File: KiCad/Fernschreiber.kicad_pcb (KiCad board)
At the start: 2 copper layers, 100 x 100 mm, 40 parts, among them J1 Teleprinter, J10 Test_Conn_write, J11 Test_Conn_Lesen_b_opto, J12 Conn_01x05_Male, J2 Step-Up, J3 18,19,23,3V3,GND, J4 12,13,14,3V3,GND, J5 TX,RX,3V3,GND, J6 5V, J7 Test_Conn_3V3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

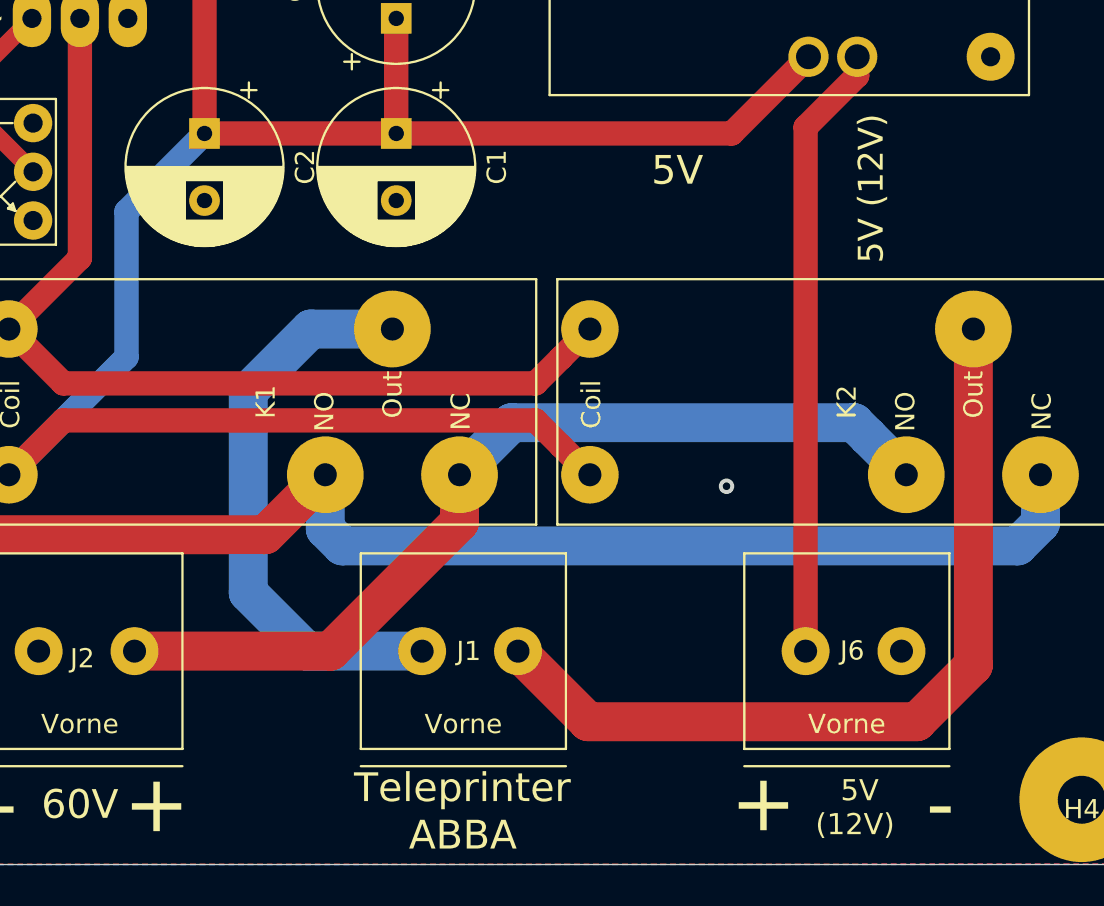
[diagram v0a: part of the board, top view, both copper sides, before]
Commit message: changed connector Position
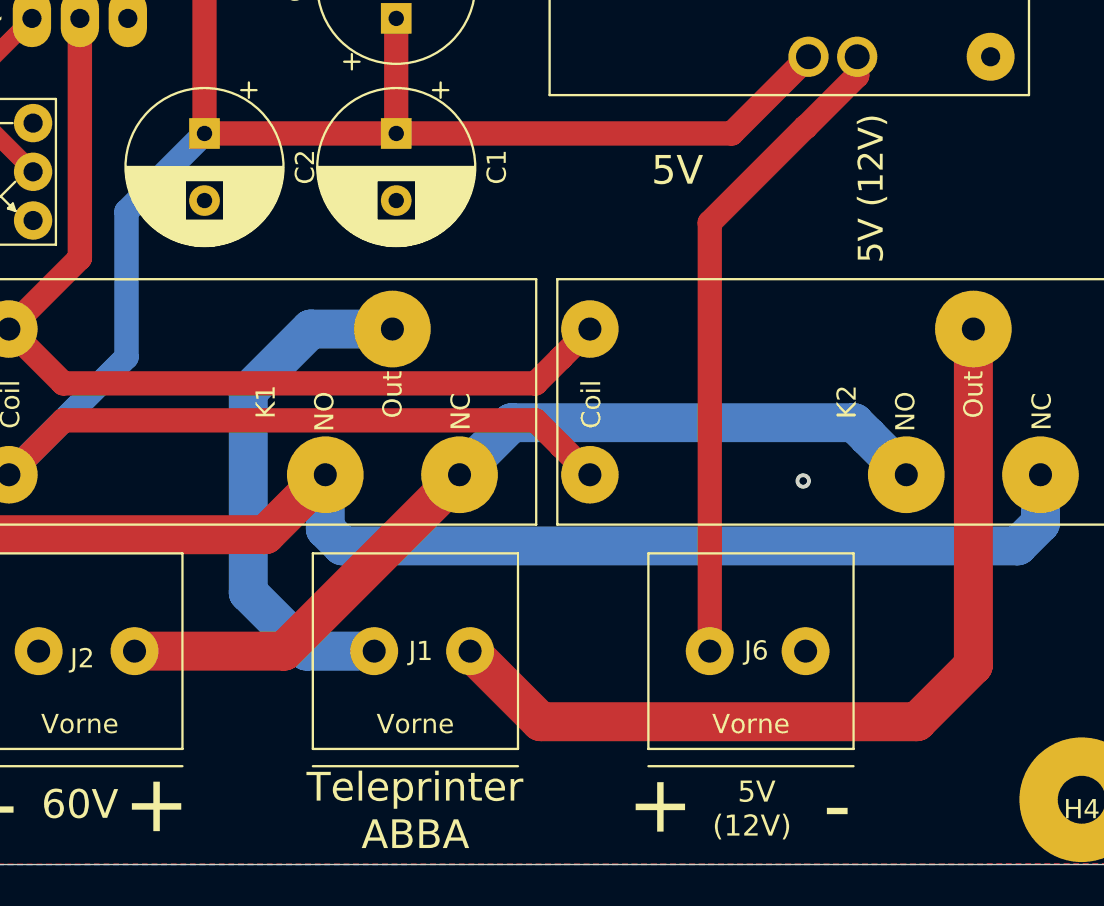
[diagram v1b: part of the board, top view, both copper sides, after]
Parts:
- moved J6 5.00 mm to (125.0, 130.0)
- moved J1 2.50 mm to (107.5, 130.0)
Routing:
- net Net-(J1-Pad1): track 29.7 -> 27.2 mm
- net Net-(J1-Pad2): track 44.0 -> 46.5 mm
- net /5V_12V: track 32.1 -> 34.2 mm
- net /Step-up_input: track 47.8 -> 46.3 mm
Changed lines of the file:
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@@
     (thickness 1.6)
     (drawings 37)
-    (tracks 158)
+    (tracks 159)
     (zones 0)
     (modules 40)
@@
   )
   (layers
-    (0 F.Cu signal hide)
-    (31 B.Cu signal hide)
-    (32 B.Adhes user hide)
-    (33 F.Adhes user hide)
+    (0 F.Cu signal)
+    (31 B.Cu signal)
+    (32 B.Adhes user)
+    (33 F.Adhes user)
     (34 B.Paste user)
-    (35 F.Paste user hide)
+    (35 F.Paste user)
     (36 B.SilkS user)
     (37 F.SilkS user)
@@
     (40 Dwgs.User user hide)
     (41 Cmts.User user hide)
-    (42 Eco1.User user hide)
-    (43 Eco2.User user hide)
+    (42 Eco1.User user)
+    (43 Eco2.User user)
     (44 Edge.Cuts user)
     (45 Margin user hide)
@@
   )
   (setup
-    (last_trace_width 0.25)
+    (last_trace_width 2.032)
     (user_trace_width 0.889)
     (user_trace_width 1.27)
@@
       (drillshape 0)
       (scaleselection 1)
-      (outputdirectory "Gerber/"))
+      (outputdirectory "Gerber_rev2/"))
   )
   (net 0 "")
@@
   (module Fernschreiber:HTR_Logo (layer F.Cu)
     (at 65.95 62.925)
-    (fp_text reference G*** (at -0.254 -14.097) (layer F.SilkS) hide
+    (fp_text reference G*** (at -0.254 -14.097) (layer Dwgs.User) hide
       (effects (font (size 1.524 1.524) (thickness 0.3)))
     )
-    (fp_text value LOGO (at -0.127 -12.065) (layer F.SilkS) hide
+    (fp_text value LOGO (at -0.127 -12.065) (layer Dwgs.User) hide
       (effects (font (size 1.524 1.524) (thickness 0.3)))
     )
@@
   (module Fernschreiber:Signatur (layer F.Cu)
     (at 128.225 46.675 90)
-    (fp_text reference G*** (at 0 0 90) (layer F.SilkS) hide
+    (fp_text reference G*** (at 0 0 90) (layer Dwgs.User) hide
       (effects (font (size 1.524 1.524) (thickness 0.3)))
     )
-    (fp_text value LOGO (at 0.75 0 90) (layer F.SilkS) hide
+    (fp_text value LOGO (at 0.75 0 90) (layer Dwgs.User) hide
       (effects (font (size 1.524 1.524) (thickness 0.3)))
     )
@@
   )
   (module "Fernschreiber:DECA MB310-500M02 Schraubklemmblock" (layer F.Cu)
-    (at 130 130)
+    (at 125 130)
     (fp_text reference J6 (at 0.2794 -0.0254) (layer F.SilkS)
       (effects (font (size 1 1) (thickness 0.15)))
@@
   )
   (module "Fernschreiber:DECA MB310-500M02 Schraubklemmblock" (layer F.Cu)
-    (at 110 130)
+    (at 107.5 130)
     (fp_text reference J1 (at 0.2794 0) (layer F.SilkS)
       (effects (font (size 1 1) (thickness 0.15)))
@@
     )
   )
-  (gr_text ABBA (at 109.975 139.6) (layer F.SilkS)
+  (gr_text ABBA (at 107.5 139.575) (layer F.SilkS)
     (effects (font (size 1.5 1.5) (thickness 0.3)))
   )
@@
     (effects (font (size 3 3) (thickness 0.5)))
   )
-  (gr_text - (at 134.875 138) (layer F.SilkS)
+  (gr_text - (at 129.5 138.075) (layer F.SilkS)
     (effects (font (size 3 3) (thickness 0.5)))
   )
-  (gr_text + (at 125.65 137.95) (layer F.SilkS)
+  (gr_text + (at 120.275 138.025) (layer F.SilkS)
     (effects (font (size 3 3) (thickness 0.5)))
   )
@@
     (effects (font (size 1.5 1.5) (thickness 0.3)))
   )
-  (gr_text Teleprinter (at 109.95 137.125) (layer F.SilkS)
+  (gr_text Teleprinter (at 107.475 137.1) (layer F.SilkS)
     (effects (font (size 1.5 1.5) (thickness 0.3)))
   )
@@
     (effects (font (size 1.5 1.5) (thickness 0.3)) (justify left mirror))
   )
-  (gr_text " 5V \n(12V)" (at 130.429 138.1506) (layer F.SilkS)
+  (gr_text " 5V \n(12V)" (at 125.054 138.2256) (layer F.SilkS)
     (effects (font (size 1.1 1.1) (thickness 0.25)))
   )
@@
   (segment (start 59.59 51.2) (end 59.5964 51.2064) (width 0.889) (layer B.Cu) (net 1))
   (via (at 87.45 66.9) (size 0.8) (drill 0.4) (layers F.Cu B.Cu) (net 1))
-  (via (at 123.725 121.4) (size 0.8) (drill 0.4) (layers F.Cu B.Cu) (net 1))
+  (via (at 127.725 121.125) (size 0.8) (drill 0.4) (layers F.Cu B.Cu) (net 1))
   (segment (start 95.504 43.5) (end 95.504 45.2882) (width 0.889) (layer F.Cu) (net 2))
   (segment (start 95.504 45.2882) (end 96.1136 45.8978) (width 0.889) (layer F.Cu) (net 2))
@@
   (segment (start 74.3704 79.425) (end 82.5 87.5546) (width 0.889) (layer B.Cu) (net 2))
   (segment (start 59.875 79.425) (end 74.3704 79.425) (width 0.889) (layer B.Cu) (net 2))
-  (segment (start 101.8314 130) (end 107.85 130) (width 2.032) (layer B.Cu) (net 3))
   (segment (start 98.7806 126.9492) (end 101.8314 130) (width 2.032) (layer B.Cu) (net 3))
   (segment (start 98.7806 116.459) (end 98.7806 126.9492) (width 2.032) (layer B.Cu) (net 3))
   (segment (start 106.3 113.2) (end 102.0396 113.2) (width 2.032) (layer B.Cu) (net 3))
   (segment (start 102.0396 113.2) (end 98.7806 116.459) (width 2.032) (layer B.Cu) (net 3))
+  (segment (start 105.35 130) (end 101.8314 130) (width 2.032) (layer B.Cu) (net 3))
   (segment (start 87.5 89.3) (end 87.5 97) (width 1.27) (layer F.Cu) (net 4))
   (segment (start 96.5 80.3) (end 87.5 89.3) (width 1.27) (layer F.Cu) (net 4))
@@
   (segment (start 140.1 123.3234) (end 140.1 120.8) (width 2.032) (layer B.Cu) (net 18))
   (segment (start 102.8 123.628427) (end 103.682373 124.5108) (width 2.032) (layer B.Cu) (net 18))
-  (segment (start 112.85 130.025) (end 112.85 130) (width 2.032) (layer F.Cu) (net 19))
-  (segment (start 116.5052 133.6802) (end 112.85 130.025) (width 2.032) (layer F.Cu) (net 19))
-  (segment (start 133.6548 133.6802) (end 116.5052 133.6802) (width 2.032) (layer F.Cu) (net 19))
   (segment (start 136.6 113.2) (end 136.6 130.735) (width 2.032) (layer F.Cu) (net 19))
+  (segment (start 114.0302 133.6802) (end 110.35 130) (width 2.032) (layer F.Cu) (net 19))
+  (segment (start 133.6548 133.6802) (end 114.0302 133.6802) (width 2.032) (layer F.Cu) (net 19))
   (segment (start 136.6 130.735) (end 133.6548 133.6802) (width 2.032) (layer F.Cu) (net 19))
   (segment (start 112.516001 118.083999) (end 130.383999 118.083999) (width 2.032) (layer B.Cu) (net 20))
@@
   (segment (start 130.383999 118.083999) (end 131.100001 118.800001) (width 2.032) (layer B.Cu) (net 20))
   (segment (start 109.8 120.8) (end 112.516001 118.083999) (width 2.032) (layer B.Cu) (net 20))
-  (segment (start 109.8 123.2704) (end 109.8 120.8) (width 2.032) (layer F.Cu) (net 20))
-  (segment (start 92.85 130) (end 103.0704 130) (width 2.032) (layer F.Cu) (net 20))
-  (segment (start 103.0704 130) (end 109.8 123.2704) (width 2.032) (layer F.Cu) (net 20))
+  (segment (start 92.85 130) (end 100.65 130) (width 2.032) (layer F.Cu) (net 20))
+  (segment (start 109.8 120.85) (end 109.8 120.8) (width 2.032) (layer F.Cu) (net 20))
+  (segment (start 100.65 130) (end 109.8 120.85) (width 2.032) (layer F.Cu) (net 20))
   (segment (start 67.2164 97.9664) (end 67.25 98) (width 0.889) (layer F.Cu) (net 21))
   (segment (start 67.2164 76.6064) (end 67.2164 97.9664) (width 0.889) (layer F.Cu) (net 21))
@@
   (segment (start 47.9746 117.9348) (end 47.9746 122.6848) (width 2.032) (layer F.Cu) (net 26) (status 30))
   (segment (start 130.54 99.985) (end 130.54 99) (width 1.27) (layer F.Cu) (net 27))
-  (segment (start 127.85 130) (end 127.85 102.675) (width 1.27) (layer F.Cu) (net 27))
   (segment (start 127.85 102.675) (end 130.54 99.985) (width 1.27) (layer F.Cu) (net 27))
+  (segment (start 122.85 130) (end 122.85 107.65) (width 1.27) (layer F.Cu) (net 27))
+  (segment (start 127.825 102.675) (end 127.85 102.675) (width 1.27) (layer F.Cu) (net 27))
+  (segment (start 122.85 107.65) (end 127.825 102.675) (width 1.27) (layer F.Cu) (net 27))
   (zone (net 1) (net_name GND) (layer F.Cu) (hatch edge 0.508)
     (connect_pads (clearance 0.5))
